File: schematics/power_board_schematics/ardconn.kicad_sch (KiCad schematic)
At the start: 2 parts

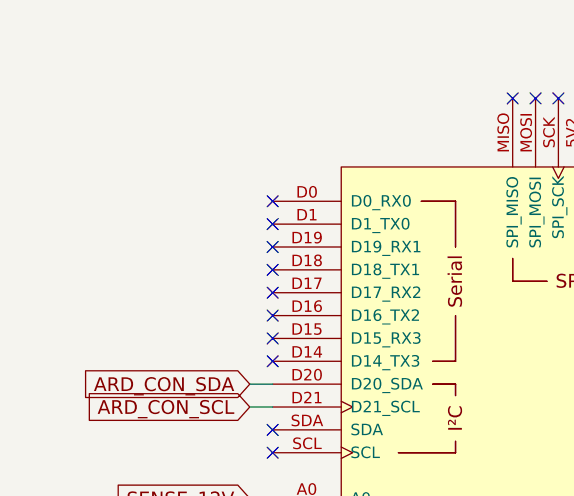
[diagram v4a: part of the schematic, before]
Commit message: Add UART connector to Towerside Power Board schematic
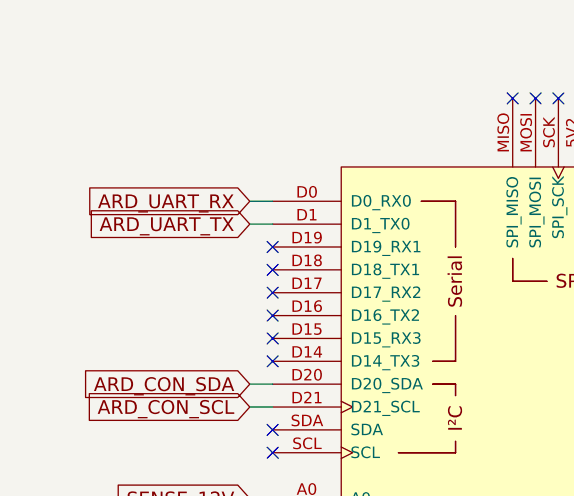
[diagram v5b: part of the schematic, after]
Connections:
- net ARD_UART_RX: now reaches XA1.D0 (D0_RX0)
- net ARD_UART_TX: now reaches XA1.D1 (D1_TX0)
- no-connect marks 62 -> 60
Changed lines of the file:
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@@
   (no_connect (at 60.96 68.58))
   (no_connect (at 60.96 66.04))
-  (no_connect (at 60.96 63.5))
-  (no_connect (at 60.96 60.96))
   (no_connect (at 127 160.02))
   (no_connect (at 127 157.48))
@@
     (stroke (width 0) (type default) (color 0 0 0 0))
   )
+  (wire (pts (xy 58.42 63.5) (xy 60.96 63.5))
+    (stroke (width 0) (type default) (color 0 0 0 0))
+  )
   (wire (pts (xy 58.42 154.94) (xy 58.42 152.4))
     (stroke (width 0) (type default) (color 0 0 0 0))
@@
   )
   (wire (pts (xy 58.42 96.52) (xy 60.96 96.52))
+    (stroke (width 0) (type default) (color 0 0 0 0))
+  )
+  (wire (pts (xy 58.42 60.96) (xy 60.96 60.96))
     (stroke (width 0) (type default) (color 0 0 0 0))
   )
@@
     )
   )
+  (global_label "ARD_UART_TX" (shape input) (at 58.42 63.5 180) (fields_autoplaced)
+    (effects (font (size 1.524 1.524)) (justify right))
+    (property "Intersheet References" "${INTERSHEET_REFS}" (id 0) (at 40.754 63.4048 0)
+      (effects (font (size 1.524 1.524)) (justify right) hide)
+    )
+  )
   (global_label "Sevenseg_D1" (shape input) (at 129.54 144.78 0) (fields_autoplaced)
     (effects (font (size 1.524 1.524)) (justify left))
@@
     )
   )
+  (global_label "ARD_UART_RX" (shape input) (at 58.42 60.96 180) (fields_autoplaced)
+    (effects (font (size 1.524 1.524)) (justify right))
+    (property "Intersheet References" "${INTERSHEET_REFS}" (id 0) (at 40.3911 60.8648 0)
+      (effects (font (size 1.524 1.524)) (justify right) hide)
+    )
+  )

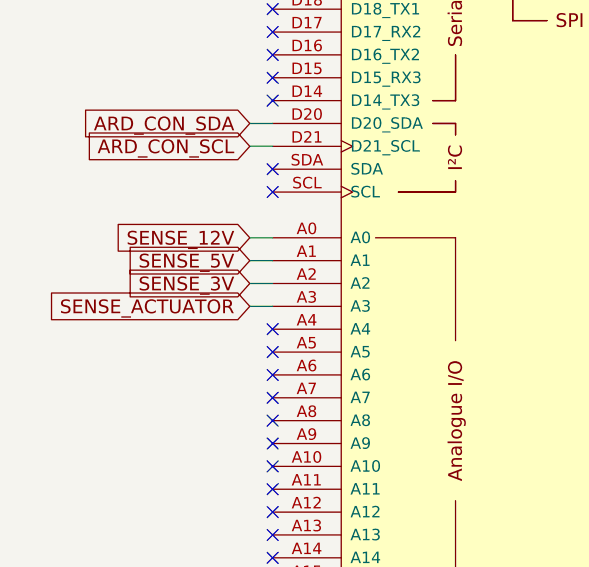
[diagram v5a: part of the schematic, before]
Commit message: Move 12v sensing from analog input A0 to A4 on Towerside Power Board
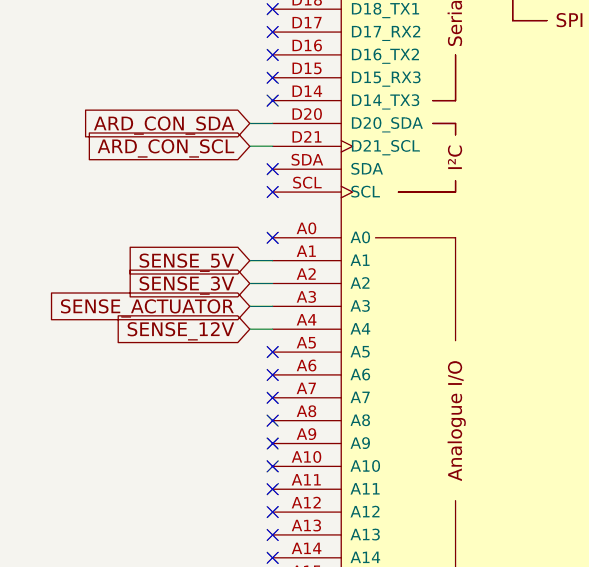
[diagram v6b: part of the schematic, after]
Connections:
- net SENSE_12V: now also XA1.A4; no longer XA1.A0
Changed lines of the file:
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@@
   (no_connect (at 60.96 68.58))
   (no_connect (at 60.96 66.04))
+  (no_connect (at 60.96 93.98))
   (no_connect (at 127 160.02))
   (no_connect (at 127 157.48))
@@
   (no_connect (at 60.96 109.22))
   (no_connect (at 60.96 106.68))
-  (no_connect (at 60.96 104.14))
   (no_connect (at 60.96 88.9))
   (no_connect (at 127 104.14))
@@
     (stroke (width 0) (type default) (color 0 0 0 0))
   )
+  (wire (pts (xy 58.42 104.14) (xy 60.96 104.14))
+    (stroke (width 0) (type default) (color 0 0 0 0))
+  )
   (wire (pts (xy 58.42 152.4) (xy 58.42 149.86))
     (stroke (width 0) (type default) (color 0 0 0 0))
@@
   )
   (wire (pts (xy 97.79 49.53) (xy 97.79 45.72))
-    (stroke (width 0) (type default) (color 0 0 0 0))
-  )
-  (wire (pts (xy 58.42 93.98) (xy 60.96 93.98))
     (stroke (width 0) (type default) (color 0 0 0 0))
   )
@@
     )
   )
-  (global_label "SENSE_12V" (shape input) (at 58.42 93.98 180) (fields_autoplaced)
-    (effects (font (size 1.524 1.524)) (justify right))
-    (property "Intersheet References" "${INTERSHEET_REFS}" (id 0) (at 43.0037 93.8848 0)
+  (global_label "SENSE_12V" (shape input) (at 58.42 104.14 180) (fields_autoplaced)
+    (effects (font (size 1.524 1.524)) (justify right))
+    (property "Intersheet References" "${INTERSHEET_REFS}" (id 0) (at 43.0037 104.0448 0)
       (effects (font (size 1.524 1.524)) (justify right) hide)
     )

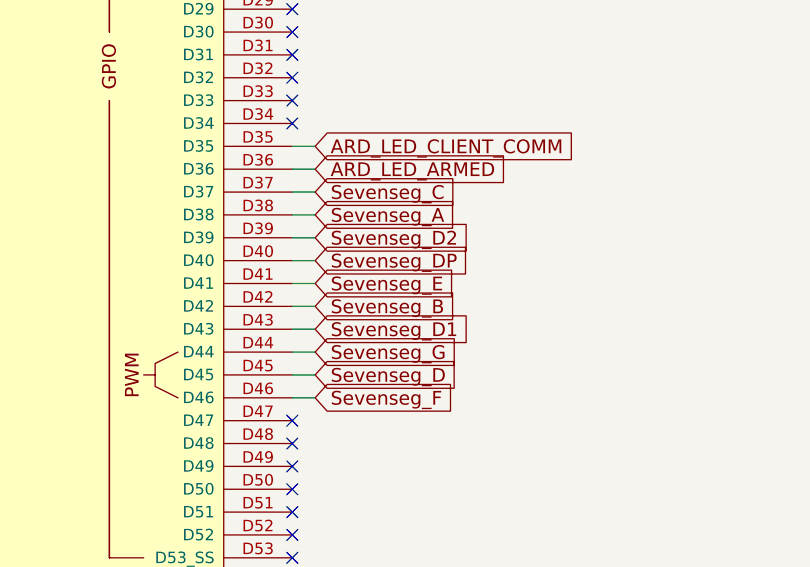
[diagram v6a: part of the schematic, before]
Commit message: Swap Sevenseg D1 and D2 label on Towerside Power Board schematics
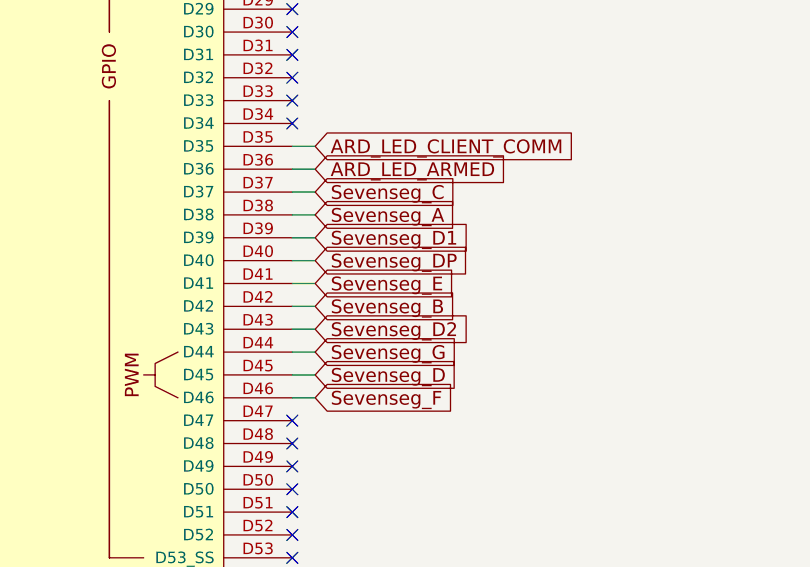
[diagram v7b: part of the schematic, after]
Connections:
- net Sevenseg_D1: now also XA1.D39; no longer XA1.D43
- net Sevenseg_D2: now also XA1.D43; no longer XA1.D39
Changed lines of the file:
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@@
     )
   )
-  (global_label "Sevenseg_D1" (shape input) (at 129.54 144.78 0) (fields_autoplaced)
+  (global_label "Sevenseg_D2" (shape input) (at 129.54 144.78 0) (fields_autoplaced)
     (effects (font (size 1.524 1.524)) (justify left))
-    (property "Intersheet References" "${INTERSHEET_REFS}" (id 0) (at 309.88 210.82 0)
-      (effects (font (size 1.27 1.27)) hide)
+    (property "Intersheet References" "${INTERSHEET_REFS}" (id 0) (at 146.9883 144.6848 0)
+      (effects (font (size 1.524 1.524)) (justify left) hide)
     )
   )
@@
     )
   )
-  (global_label "Sevenseg_D2" (shape input) (at 129.54 134.62 0) (fields_autoplaced)
+  (global_label "Sevenseg_D1" (shape input) (at 129.54 134.62 0) (fields_autoplaced)
     (effects (font (size 1.524 1.524)) (justify left))
-    (property "Intersheet References" "${INTERSHEET_REFS}" (id 0) (at 309.88 190.5 0)
-      (effects (font (size 1.27 1.27)) hide)
+    (property "Intersheet References" "${INTERSHEET_REFS}" (id 0) (at 146.9883 134.5248 0)
+      (effects (font (size 1.524 1.524)) (justify left) hide)
     )
   )

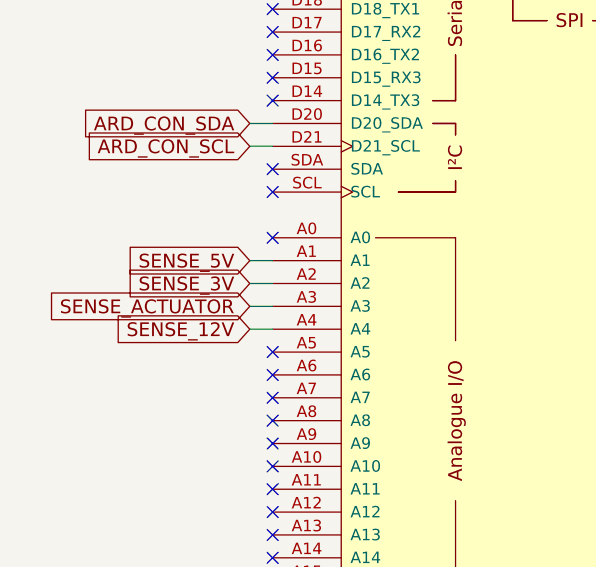
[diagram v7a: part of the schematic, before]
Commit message: Remove 3.3V circuit from Towerside Power Board
Remove 3.3V regulator
Remove 3.3V sensing
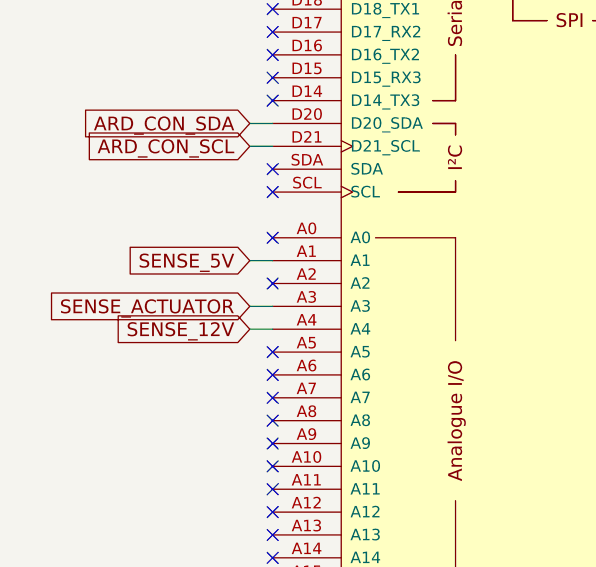
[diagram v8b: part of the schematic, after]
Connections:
- net SENSE_3V: no longer names the net of XA1.A2
- no-connect marks 60 -> 61
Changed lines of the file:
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@@
   (no_connect (at 60.96 68.58))
   (no_connect (at 60.96 66.04))
+  (no_connect (at 60.96 99.06))
   (no_connect (at 60.96 93.98))
   (no_connect (at 127 160.02))
@@
     (stroke (width 0) (type default) (color 0 0 0 0))
   )
-  (wire (pts (xy 58.42 99.06) (xy 60.96 99.06))
-    (stroke (width 0) (type default) (color 0 0 0 0))
-  )
   (wire (pts (xy 129.54 137.16) (xy 127 137.16))
     (stroke (width 0) (type default) (color 0 0 0 0))
@@
       (effects (font (size 1.524 1.524)) (justify right) hide)
     )
-  )
-  (global_label "SENSE_3V" (shape input) (at 58.42 99.06 180) (fields_autoplaced)
-    (effects (font (size 1.524 1.524)) (justify right))
-    (property "Intersheet References" "${INTERSHEET_REFS}" (id 0) (at 44.4551 98.9648 0)
-      (effects (font (size 1.524 1.524)) (justify right) hide)
-    )
